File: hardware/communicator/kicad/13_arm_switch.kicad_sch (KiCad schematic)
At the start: 8 parts, among them J30 TX_ARM normally OPEN, U33 SN74LVC1G11DCKR, U34 SN74LVC1G04DBVR, U35 SN74LVC2G17DCKR

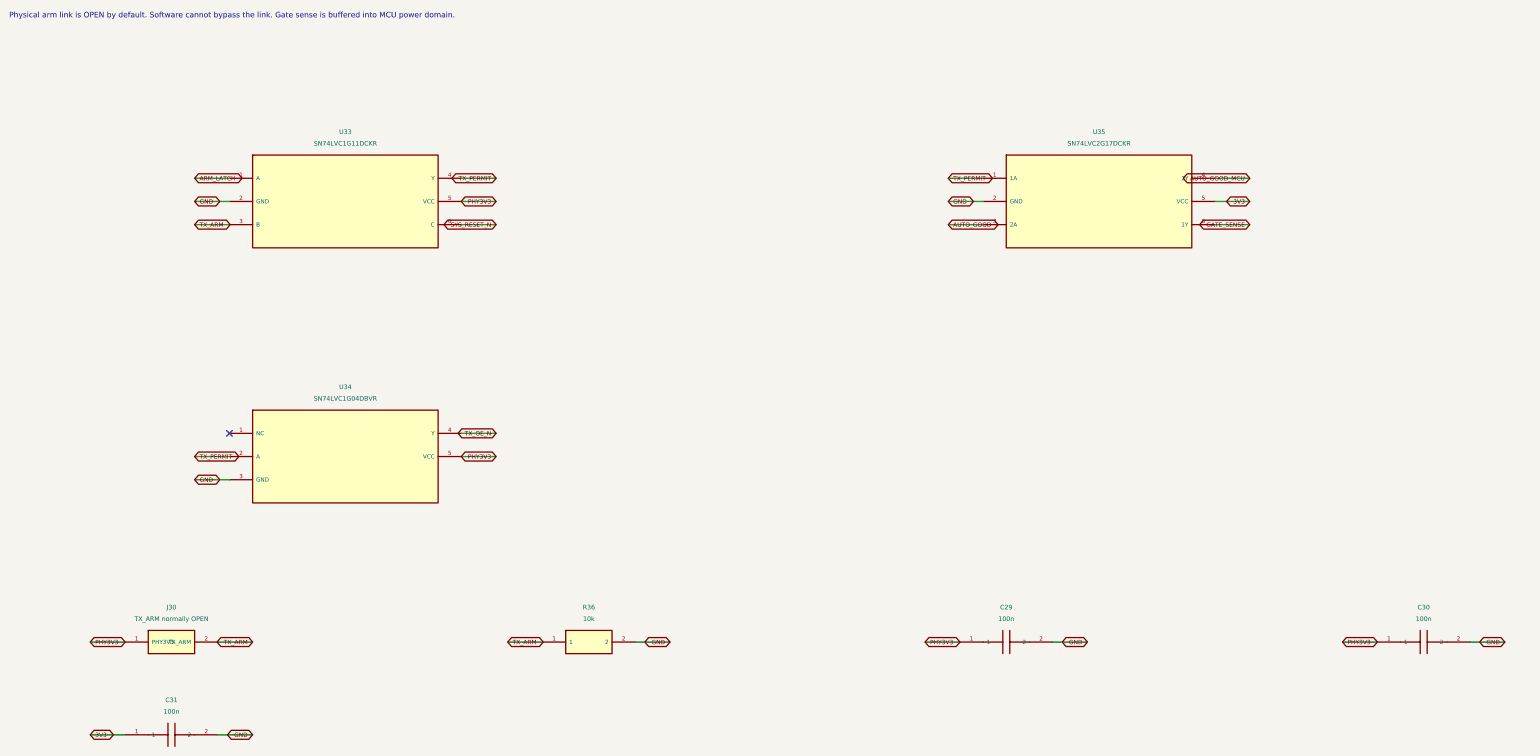
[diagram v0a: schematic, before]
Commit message: feat: add R1 detailed hardware and navigation protocol review candidate
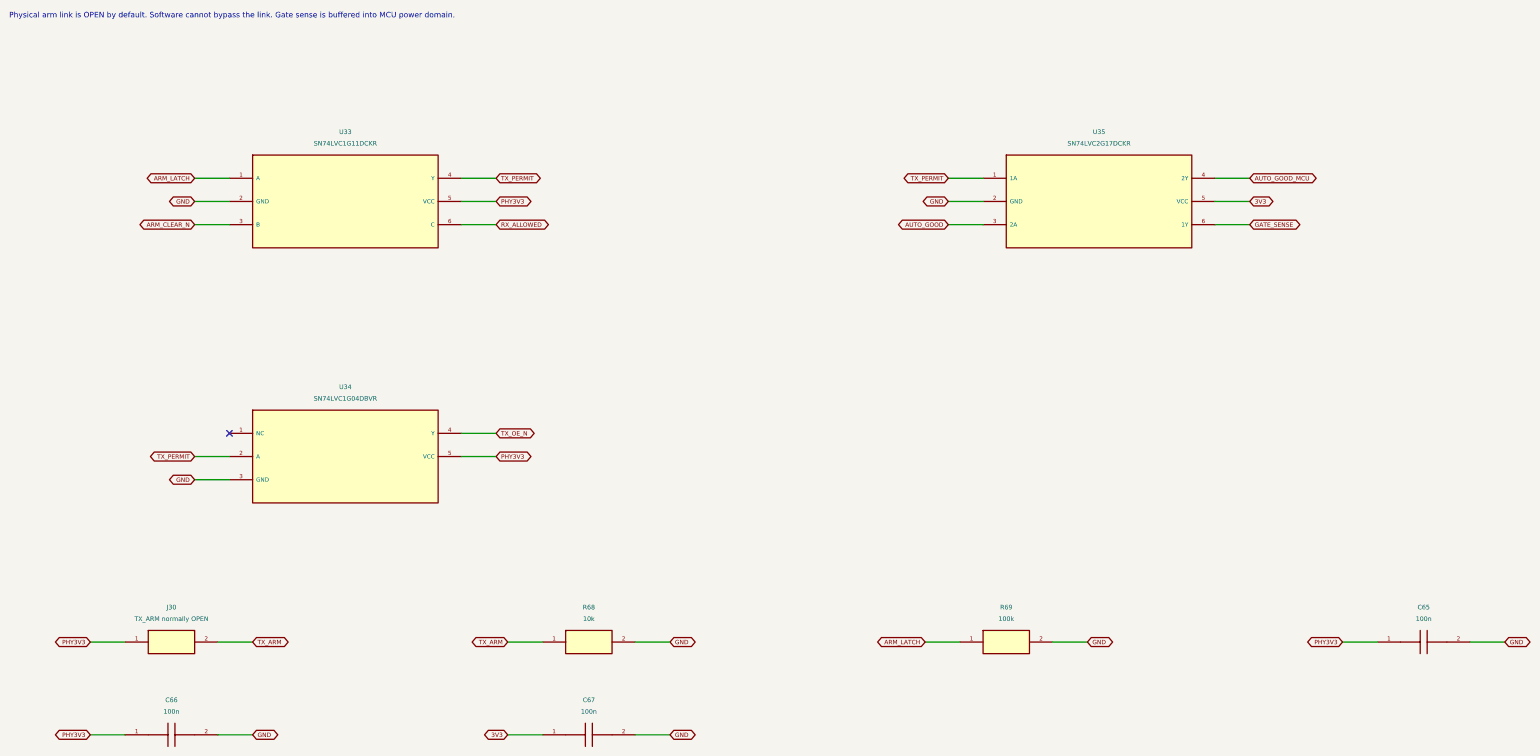
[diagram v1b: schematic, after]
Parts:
- removed C29: 100n, CANView:Capacitor_SMD__C_0402_1005Metric, symbol CANView:CANView_communicator_C29
- removed C30: 100n, CANView:Capacitor_SMD__C_0402_1005Metric, symbol CANView:CANView_communicator_C30
- removed C31: 100n, CANView:Capacitor_SMD__C_0402_1005Metric, symbol CANView:CANView_communicator_C31
- removed R36: 10k, CANView:Resistor_SMD__R_0402_1005Metric, symbol CANView:CANView_communicator_R36
- added C65: 100n, CANView:Capacitor_SMD__C_0402_1005Metric, symbol CANView:CANView_communicator_C65
- added C66: 100n, CANView:Capacitor_SMD__C_0402_1005Metric, symbol CANView:CANView_communicator_C66
- added C67: 100n, CANView:Capacitor_SMD__C_0402_1005Metric, symbol CANView:CANView_communicator_C67
- added R68: 10k, CANView:Resistor_SMD__R_0402_1005Metric, symbol CANView:CANView_communicator_R68
- added R69: 100k, CANView:Resistor_SMD__R_0402_1005Metric, symbol CANView:CANView_communicator_R69
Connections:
- net 3V3: now also C67.1
- net ARM_LATCH: now also R69.1
- net GND: now also C65.2, C66.2, C67.2, R68.2, R69.2
- net PHY3V3: now also C65.1, C66.1
- net TX_ARM: now also R68.1; no longer U33.3 (B)
- net SYS_RESET_N renamed RX_ALLOWED
- new net ARM_CLEAR_N: U33.3 (B)

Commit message: fix: close hardware rail-fault paths and sensor contract gaps
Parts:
- removed C65: 100n, CANView:Capacitor_SMD__C_0402_1005Metric, symbol CANView:CANView_communicator_C65
- removed C66: 100n, CANView:Capacitor_SMD__C_0402_1005Metric, symbol CANView:CANView_communicator_C66
- removed R68: 10k, CANView:Resistor_SMD__R_0402_1005Metric, symbol CANView:CANView_communicator_R68
- removed R69: 100k, CANView:Resistor_SMD__R_0402_1005Metric, symbol CANView:CANView_communicator_R69
- added C68: 100n, CANView:Capacitor_SMD__C_0402_1005Metric, symbol CANView:CANView_communicator_C68
- added C69: 100n, CANView:Capacitor_SMD__C_0402_1005Metric, symbol CANView:CANView_communicator_C69
- added R71: 10k, CANView:Resistor_SMD__R_0402_1005Metric, symbol CANView:CANView_communicator_R71
- added R72: 100k, CANView:Resistor_SMD__R_0402_1005Metric, symbol CANView:CANView_communicator_R72
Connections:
- net 3V3: now also C69.1; no longer C67.1
- net ARM_LATCH: now also R72.1
- net GND: now also C68.2, C69.2, R71.2, R72.2
- net PHY3V3: now also C67.1, C68.1
- net TX_ARM: now also R71.1
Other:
- moved on the sheet: C67
